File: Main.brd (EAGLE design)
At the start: 100 x 80 mm, 11 parts, among them U2 LM 1084 IT5,0, U3 LM 1084 IT3,3, X1 12V

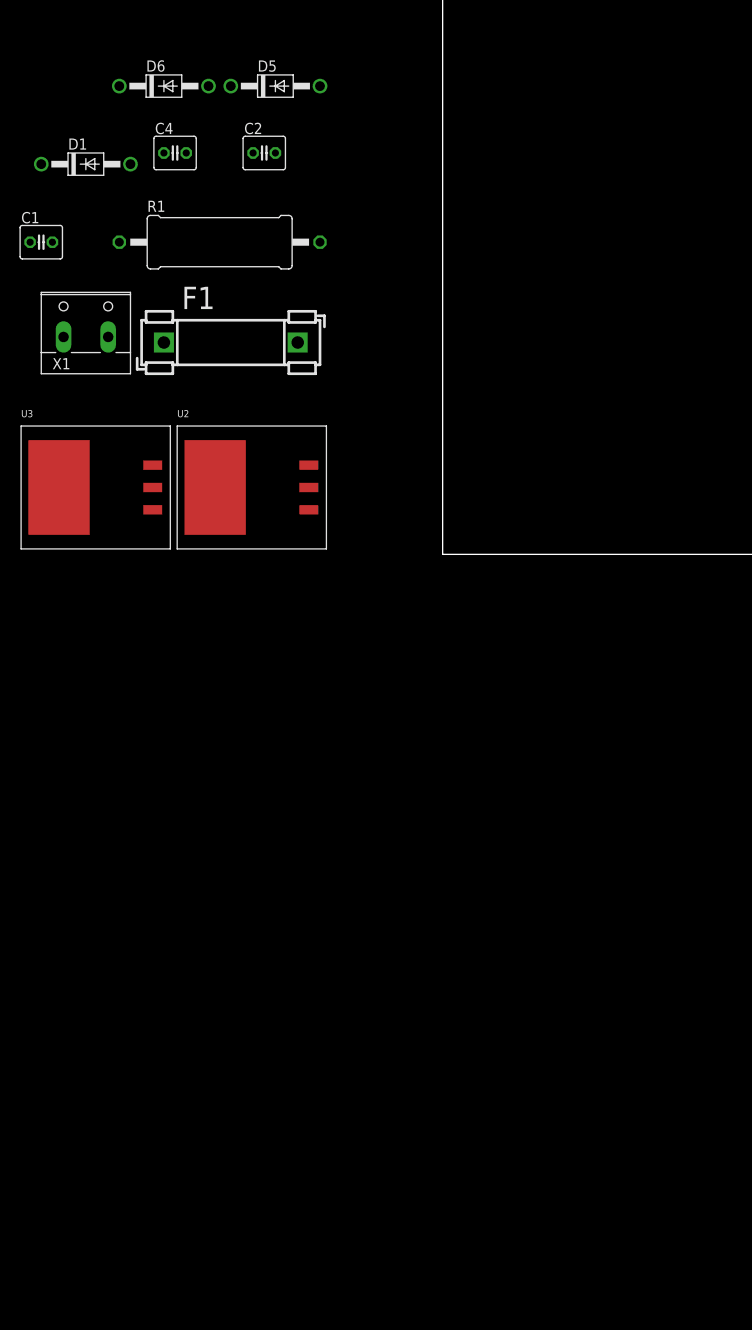
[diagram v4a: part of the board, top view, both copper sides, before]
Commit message: added first motor driver
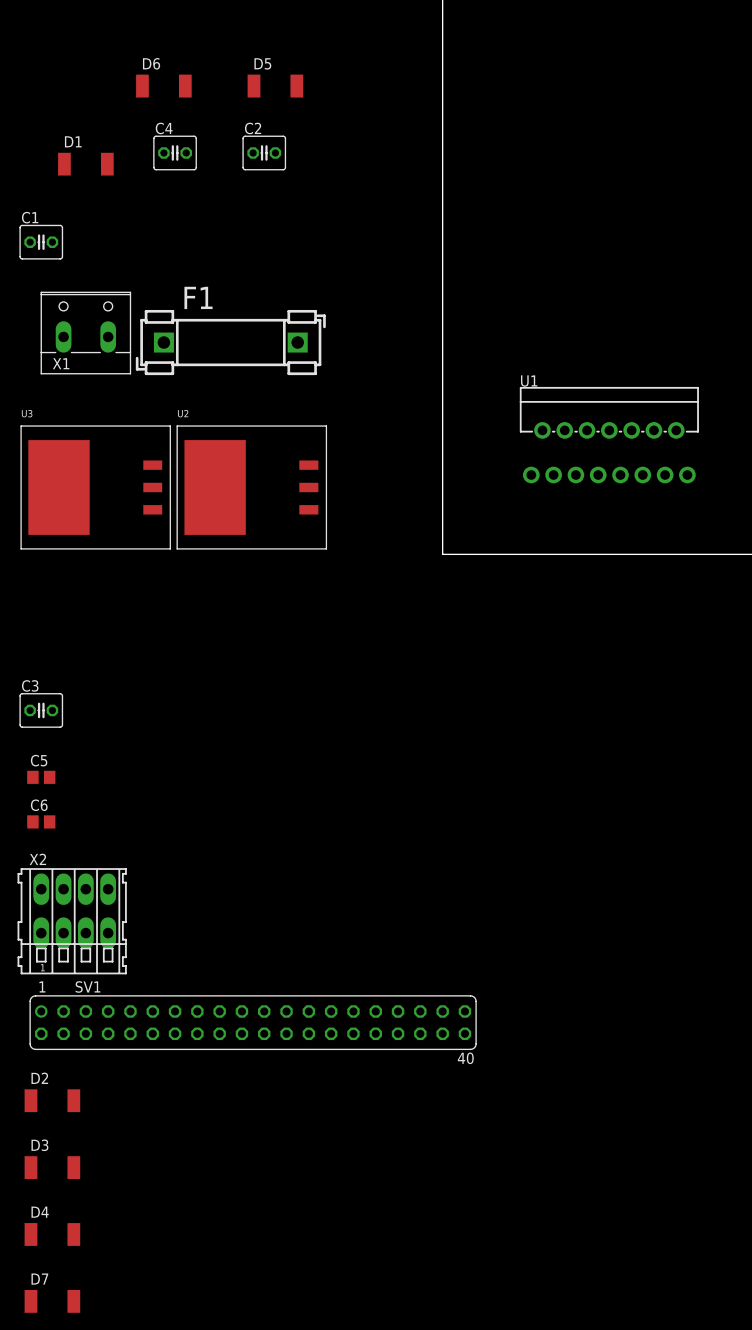
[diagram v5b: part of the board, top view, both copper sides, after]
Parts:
- removed R1: 4711, resistor:0617/22
- added C3: 10uF Tant., rcl:C025-040X050
- added C5, C6: 100nF, rcl:C0805
- added D2, D3, D4, D7: 1N4007, semicon-smd-ipc:MELF-MLL41
- added SV1: (no value), con-lsta:FE20-2
- added U1: L298, SparkFun-PowerIC:MULTIWATT15
- added X2: (no value), con-wago255:233-504
- D1, D5, D6: value 1N4004 -> 1N4007; device diode:DO41-10 -> semicon-smd-ipc:MELF-MLL41
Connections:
- new net ML_A: U1.12, U1.5
- new net ML_B: U1.10, U1.7
- new net ML_PWM: U1.11, U1.6
- new net N$4: D3.2, D4.1, U1.13, U1.3
- new net N$5: D2.2, D7.1, U1.14, U1.2
- net +12V: now also C3.1, C5.1, D1.1, D2.1, D3.1, D5.1, D6.1, U1.4; no longer D1.C, D5.C, D6.C, R1.1
- net +3.3V: now also D6.2; no longer D6.A
- net +5V: now also C6.1, D5.2, U1.9; no longer D5.A
- net GND: now also C3.2, C5.2, C6.2, D1.2, D4.2, D7.2, SV1.6, U1.8; no longer D1.A, R1.2

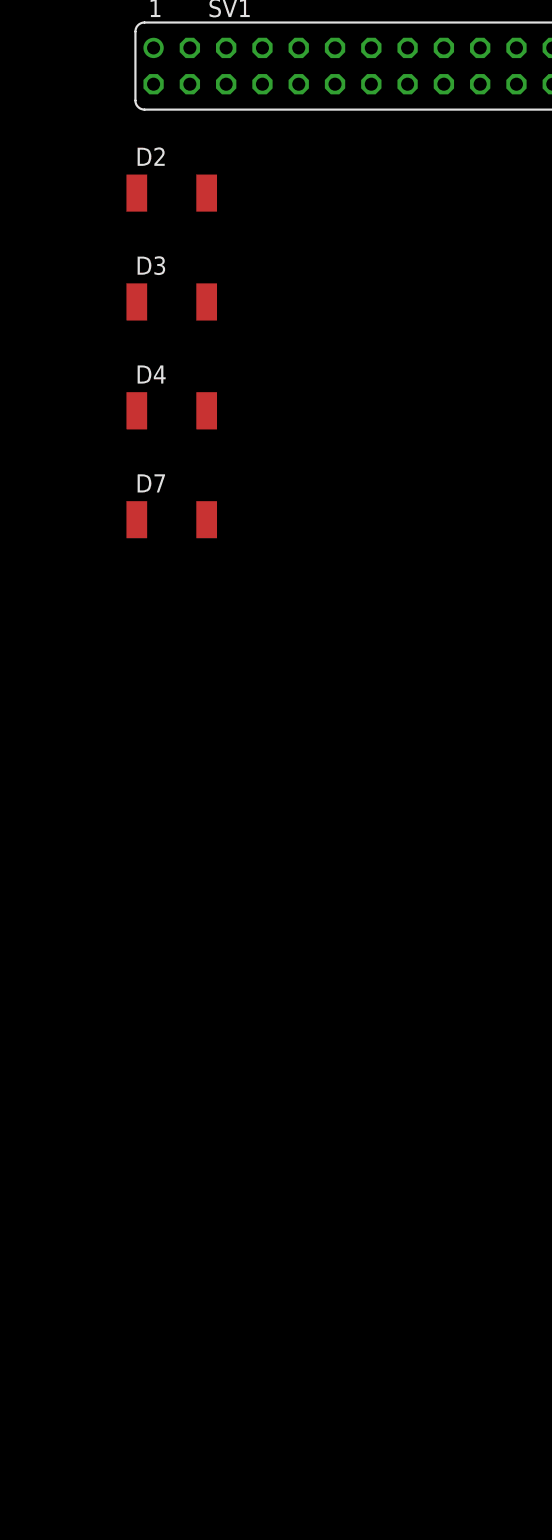
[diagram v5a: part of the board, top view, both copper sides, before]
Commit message: added second motor driver and fixed protction diodes
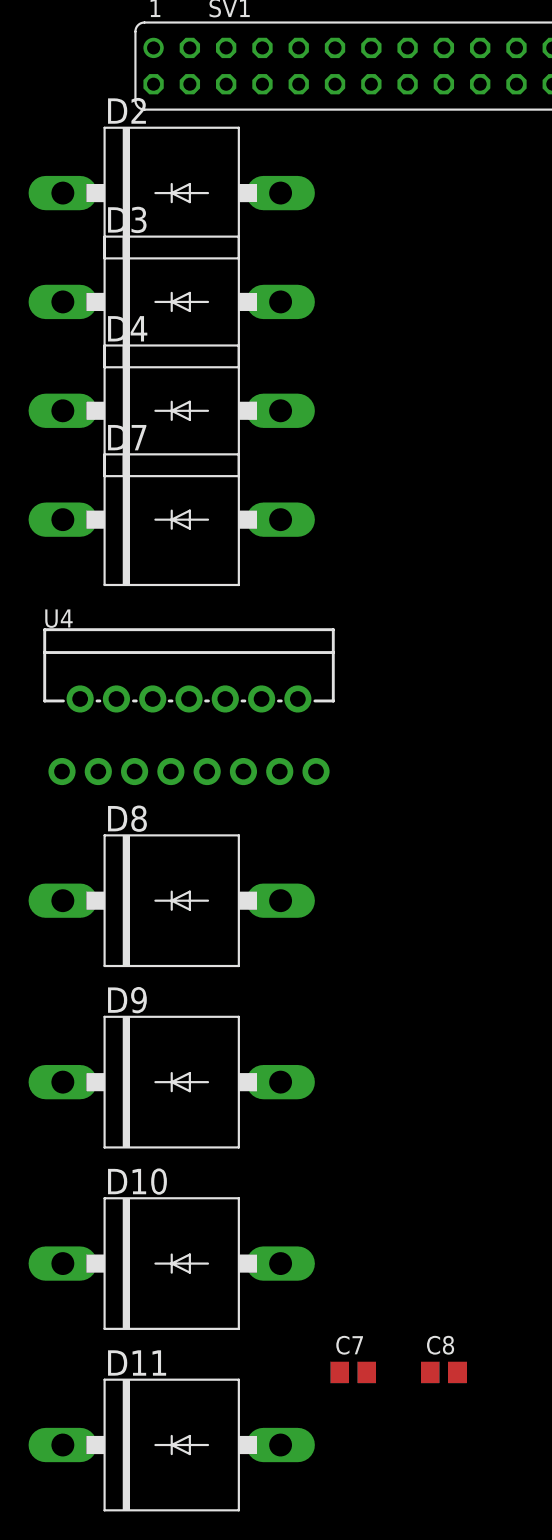
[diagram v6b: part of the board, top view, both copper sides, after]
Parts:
- added C7, C8: 100nF, rcl:C0805
- added D10, D11, D8, D9: 1N4007, diode:P6-15
- added U4: L298, SparkFun-PowerIC:MULTIWATT15
- D2, D3, D4, D7: device semicon-smd-ipc:MELF-MLL41 -> diode:P6-15
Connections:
- removed net N$4: D3.2, D4.1, U1.13, U1.3
- removed net N$5: D2.2, D7.1, U1.14, U1.2
- new net ML_OUT_A: D2.A, D7.C, U1.14, U1.2, X2.A1
- new net ML_OUT_B: D3.A, D4.C, U1.13, U1.3, X2.A2
- new net MR_A: U4.12, U4.5
- new net MR_B: U4.10, U4.7
- new net MR_OUT_A: D11.C, D8.A, U4.14, U4.2, X2.A3
- new net MR_OUT_B: D10.C, D9.A, U4.13, U4.3, X2.A4
- new net MR_PWM: U4.11, U4.6
- net +12V: now also C7.1, D2.C, D3.C, D8.C, D9.C, U4.4; no longer D2.1, D3.1
- net +5V: now also C8.1, U4.9
- net GND: now also C7.2, C8.2, D10.A, D11.A, D4.A, D7.A, U4.8; no longer D4.2, D7.2
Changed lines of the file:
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@@
 <attribute name="OC_FARNELL" value="unknown" x="-21.59" y="-53.34" size="1.778" layer="27" display="off"/>
 </element>
-<element name="D2" library="semicon-smd-ipc" package="MELF-MLL41" value="1N4007" x="-44.45" y="-62.23"/>
-<element name="D3" library="semicon-smd-ipc" package="MELF-MLL41" value="1N4007" x="-44.45" y="-69.85"/>
-<element name="D4" library="semicon-smd-ipc" package="MELF-MLL41" value="1N4007" x="-44.45" y="-77.47"/>
-<element name="D7" library="semicon-smd-ipc" package="MELF-MLL41" value="1N4007" x="-44.45" y="-85.09"/>
+<element name="D2" library="diode" package="P6-15" value="1N4007" x="-44.45" y="-62.23"/>
+<element name="D3" library="diode" package="P6-15" value="1N4007" x="-44.45" y="-69.85"/>
+<element name="D4" library="diode" package="P6-15" value="1N4007" x="-44.45" y="-77.47"/>
+<element name="D7" library="diode" package="P6-15" value="1N4007" x="-44.45" y="-85.09"/>
+<element name="U4" library="SparkFun-PowerIC" package="MULTIWATT15" value="L298" x="-43.18" y="-100.33"/>
+<element name="C7" library="rcl" package="C0805" value="100nF" x="-31.75" y="-144.78"/>
+<element name="C8" library="rcl" package="C0805" value="100nF" x="-25.4" y="-144.78"/>
+<element name="D8" library="diode" package="P6-15" value="1N4007" x="-44.45" y="-111.76"/>
+<element name="D9" library="diode" package="P6-15" value="1N4007" x="-44.45" y="-124.46"/>
+<element name="D10" library="diode" package="P6-15" value="1N4007" x="-44.45" y="-137.16"/>
+<element name="D11" library="diode" package="P6-15" value="1N4007" x="-44.45" y="-149.86"/>
 </elements>
 <signals>
@@
 <contactref element="U1" pad="9"/>
 <contactref element="C6" pad="1"/>
+<contactref element="U4" pad="9"/>
+<contactref element="C8" pad="1"/>
+<wire x1="-41.97" y1="-102.72" x2="-26.35" y2="-144.78" width="0" layer="19" extent="1-1"/>
+<wire x1="-46.67" y1="-30.48" x2="-41.97" y2="-102.72" width="0" layer="19" extent="1-1"/>
 <wire x1="-25.915" y1="7.62" x2="-46.67" y2="-30.48" width="0" layer="19" extent="1-1"/>
 <wire x1="-15.24" y1="7.62" x2="-25.915" y2="7.62" width="0" layer="19" extent="1-1"/>
@@
 <contactref element="U1" pad="4"/>
 <contactref element="C5" pad="1"/>
-<contactref element="D3" pad="1"/>
-<contactref element="D2" pad="1"/>
-<wire x1="-46.895" y1="-62.23" x2="-46.895" y2="-69.85" width="0" layer="19" extent="1-1"/>
-<wire x1="-46.67" y1="-25.4" x2="-46.895" y2="-62.23" width="0" layer="19" extent="1-1"/>
+<contactref element="D3" pad="C"/>
+<contactref element="D2" pad="C"/>
+<contactref element="U4" pad="4"/>
+<contactref element="C7" pad="1"/>
+<contactref element="D9" pad="C"/>
+<contactref element="D8" pad="C"/>
+<wire x1="-52.07" y1="-124.46" x2="-32.7" y2="-144.78" width="0" layer="19" extent="1-1"/>
+<wire x1="-52.07" y1="-111.76" x2="-52.07" y2="-124.46" width="0" layer="19" extent="1-1"/>
+<wire x1="-48.32" y1="-97.64" x2="-52.07" y2="-111.76" width="0" layer="19" extent="1-1"/>
+<wire x1="-52.07" y1="-69.85" x2="-48.32" y2="-97.64" width="0" layer="19" extent="1-1"/>
+<wire x1="-52.07" y1="-62.23" x2="-52.07" y2="-69.85" width="0" layer="19" extent="1-1"/>
+<wire x1="-46.67" y1="-25.4" x2="-52.07" y2="-62.23" width="0" layer="19" extent="1-1"/>
 <wire x1="-46.99" y1="-17.78" x2="-46.67" y2="-25.4" width="0" layer="19" extent="1-1"/>
 <wire x1="-33.02" y1="10.16" x2="-46.99" y2="-17.78" width="0" layer="19" extent="1-1"/>
@@
 <contactref element="C5" pad="2"/>
 <contactref element="C6" pad="2"/>
-<contactref element="D4" pad="2"/>
-<contactref element="D7" pad="2"/>
-<wire x1="-42.005" y1="-77.47" x2="-42.005" y2="-85.09" width="0" layer="19" extent="1-1"/>
-<wire x1="-40.64" y1="-54.61" x2="-42.005" y2="-77.47" width="0" layer="19" extent="1-1"/>
+<contactref element="D4" pad="A"/>
+<contactref element="D7" pad="A"/>
+<contactref element="U4" pad="8"/>
+<contactref element="C7" pad="2"/>
+<contactref element="C8" pad="2"/>
+<contactref element="D10" pad="A"/>
+<contactref element="D11" pad="A"/>
+<wire x1="-30.8" y1="-144.78" x2="-36.83" y2="-149.86" width="0" layer="19" extent="1-1"/>
+<wire x1="-24.45" y1="-144.78" x2="-30.8" y2="-144.78" width="0" layer="19" extent="1-1"/>
+<wire x1="-36.83" y1="-137.16" x2="-30.8" y2="-144.78" width="0" layer="19" extent="1-1"/>
+<wire x1="-43.24" y1="-97.64" x2="-36.83" y2="-137.16" width="0" layer="19" extent="1-1"/>
+<wire x1="-36.83" y1="-85.09" x2="-43.24" y2="-97.64" width="0" layer="19" extent="1-1"/>
+<wire x1="-36.83" y1="-77.47" x2="-36.83" y2="-85.09" width="0" layer="19" extent="1-1"/>
+<wire x1="-40.64" y1="-54.61" x2="-36.83" y2="-77.47" width="0" layer="19" extent="1-1"/>
 <wire x1="-44.77" y1="-30.48" x2="-40.64" y2="-54.61" width="0" layer="19" extent="1-1"/>
 <wire x1="-44.77" y1="-25.4" x2="-44.77" y2="-30.48" width="0" layer="19" extent="1-1"/>
@@
 <wire x1="15.18" y1="9.04" x2="24.07" y2="14.12" width="0" layer="19" extent="1-1"/>
 </signal>
-<signal name="N$4">
-<contactref element="D3" pad="2"/>
-<contactref element="D4" pad="1"/>
+<signal name="ML_OUT_B">
+<contactref element="D3" pad="A"/>
+<contactref element="D4" pad="C"/>
 <contactref element="U1" pad="3"/>
 <contactref element="U1" pad="13"/>
-<wire x1="-42.005" y1="-69.85" x2="-46.895" y2="-77.47" width="0" layer="19" extent="1-1"/>
-<wire x1="12.64" y1="9.04" x2="-42.005" y2="-69.85" width="0" layer="19" extent="1-1"/>
+<contactref element="X2" pad="A2"/>
+<wire x1="-36.83" y1="-69.85" x2="-52.07" y2="-77.47" width="0" layer="19" extent="1-1"/>
+<wire x1="-43.18" y1="-38.14" x2="-36.83" y2="-69.85" width="0" layer="19" extent="1-1"/>
+<wire x1="12.64" y1="9.04" x2="-43.18" y2="-38.14" width="0" layer="19" extent="1-1"/>
 <wire x1="25.34" y1="9.04" x2="12.64" y2="9.04" width="0" layer="19" extent="1-1"/>
 </signal>
-<signal name="N$5">
-<contactref element="D2" pad="2"/>
-<contactref element="D7" pad="1"/>
+<signal name="ML_OUT_A">
+<contactref element="D2" pad="A"/>
+<contactref element="D7" pad="C"/>
 <contactref element="U1" pad="2"/>
 <contactref element="U1" pad="14"/>
-<wire x1="-42.005" y1="-62.23" x2="-46.895" y2="-85.09" width="0" layer="19" extent="1-1"/>
-<wire x1="11.37" y1="14.12" x2="-42.005" y2="-62.23" width="0" layer="19" extent="1-1"/>
+<contactref element="X2" pad="A1"/>
+<wire x1="-36.83" y1="-62.23" x2="-52.07" y2="-85.09" width="0" layer="19" extent="1-1"/>
+<wire x1="-45.72" y1="-38.14" x2="-36.83" y2="-62.23" width="0" layer="19" extent="1-1"/>
+<wire x1="11.37" y1="14.12" x2="-45.72" y2="-38.14" width="0" layer="19" extent="1-1"/>
 <wire x1="26.61" y1="14.12" x2="11.37" y2="14.12" width="0" layer="19" extent="1-1"/>
 </signal>
+<signal name="MR_A">
+<contactref element="U4" pad="12"/>
+<contactref element="U4" pad="5"/>
+<wire x1="-38.16" y1="-97.64" x2="-47.05" y2="-102.72" width="0" layer="19" extent="1-1"/>
+</signal>
+<signal name="MR_B">
+<contactref element="U4" pad="10"/>
+<contactref element="U4" pad="7"/>
+<wire x1="-40.7" y1="-97.64" x2="-44.51" y2="-102.72" width="0" layer="19" extent="1-1"/>
+</signal>
+<signal name="MR_PWM">
+<contactref element="U4" pad="6"/>
+<contactref element="U4" pad="11"/>
+<wire x1="-39.43" y1="-102.72" x2="-45.78" y2="-97.64" width="0" layer="19" extent="1-1"/>
+</signal>
+<signal name="MR_OUT_A">
+<contactref element="D8" pad="A"/>
+<contactref element="D11" pad="C"/>
+<contactref element="U4" pad="14"/>
+<contactref element="U4" pad="2"/>
+<contactref element="X2" pad="A3"/>
+<wire x1="-36.83" y1="-111.76" x2="-52.07" y2="-149.86" width="0" layer="19" extent="1-1"/>
+<wire x1="-35.62" y1="-97.64" x2="-36.83" y2="-111.76" width="0" layer="19" extent="1-1"/>
+<wire x1="-50.86" y1="-97.64" x2="-35.62" y2="-97.64" width="0" layer="19" extent="1-1"/>
+<wire x1="-40.64" y1="-38.14" x2="-35.62" y2="-97.64" width="0" layer="19" extent="1-1"/>
+</signal>
+<signal name="MR_OUT_B">
+<contactref element="D10" pad="C"/>
+<contactref element="U4" pad="3"/>
+<contactref element="D9" pad="A"/>
+<contactref element="U4" pad="13"/>
+<contactref element="X2" pad="A4"/>
+<wire x1="-36.83" y1="-124.46" x2="-52.07" y2="-137.16" width="0" layer="19" extent="1-1"/>
+<wire x1="-36.89" y1="-102.72" x2="-36.83" y2="-124.46" width="0" layer="19" extent="1-1"/>
+<wire x1="-49.59" y1="-102.72" x2="-36.89" y2="-102.72" width="0" layer="19" extent="1-1"/>
+<wire x1="-38.1" y1="-38.14" x2="-36.89" y2="-102.72" width="0" layer="19" extent="1-1"/>
+</signal>
 </signals>

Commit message: some routing experiments
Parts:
- U2: value LM 1084 IT5,0 -> LM 1085 IT5,0; device PP_PowerIC:TO-263-3 -> linear-technology-3:TO220S
- U3: value LM 1084 IT3,3 -> LM 1085 IT3,3; device PP_PowerIC:TO-263-3 -> linear-technology-3:TO220S
- moved C7 226.4 mm to (22.9, 74.9), turned to 180 degrees
- moved D11 223.1 mm to (67.3, 43.2)
- moved D10 220.9 mm to (67.3, 53.3)
- moved D9 218.7 mm to (67.3, 63.5)
- moved D8 216.5 mm to (67.3, 73.7)
- moved D2 191.3 mm to (90.2, 73.7)
- moved D3 189.5 mm to (90.2, 63.5)
- moved D4 187.7 mm to (90.2, 53.3)
- moved D7 185.9 mm to (90.2, 43.2)
- moved C8 178.9 mm to (52.1, 16.5)
- moved U4 153.6 mm to (67.3, 6.35), turned to 180 degrees
- moved X2 147.2 mm to (91.4, 21.6), turned to 90 degrees
- moved C5 119.1 mm to (50.8, 44.5)
- moved U3 115.5 mm to (50.8, 81.3)
- moved C3 114.9 mm to (35.6, 63.5), turned to 180 degrees
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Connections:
- net +3.3V: no longer U3.4
- net +5V: no longer U2.4
